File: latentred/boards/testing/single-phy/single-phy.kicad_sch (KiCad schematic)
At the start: 79 parts, among them J1 XILINX_JTAG, J2 RJ45, J3 QSH-030-01-L-D-A, U1 DP83867, U2 25MHZ_TBD, U3 BEL_FUSE_S558-5999-M8-F, U4 LTC3374-QFN

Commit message: single-phy: updated for v0.2 with fixed RJ45 pinout, removed SGMII clock pair, moved digital IO to 1.8V
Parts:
- removed C1, C2: 27p, azonenberg_pcb:EIA_0402_CAP_NOSILK, symbol device:C
- removed C13, C14: 0.1 uF, azonenberg_pcb:EIA_0402_CAP_NOSILK, symbol device:C
- removed L1: FERRITE_600R, azonenberg_pcb:EIA_0603_INDUCTOR_NOSILK, symbol passive-azonenberg:INDUCTOR_PWROUT
- added Q1, Q2: SSM6N58NU, azonenberg_pcb:DFN_6_0.65MM_2x2MM_GDS, symbol special-azonenberg:SSM6N58NU_DUAL_NMOS
- added R23: 33, azonenberg_pcb:EIA_0402_RES_NOSILK, symbol device:R
- added R24: 100, azonenberg_pcb:EIA_0402_RES_NOSILK, symbol device:R
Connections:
- net A2V5 is gone; now on net 2V5: C15.1, C19.1, C26.1, U1.3 (A2V5), U1.9 (A2V5)
- net PHY_CLK_25MHZ_DIV is gone; now on net PHY_CLK_25MHZ: U1.15 (XI)
- net SGMII_CLKOUT_N is gone; now on net SGMII_TX_N: J3.26 (DQ14_P)
- net SGMII_CLKOUT_P is gone; now on net SGMII_TX_P: J3.28 (DQ14_N)
- net 1V8: now also C18.1, C22.1, C25.1, C28.1, C30.1, J1.2 (Vccaux), R1.1, R12.2, R14.2, R22.2, R6.2, U1.19 (VCCIO), U1.30 (VCCIO), U1.41 (VCCIO), U2.1 (E/D#), U2.4 (Vdd)
- net 2V5: no longer C18.1, C22.1, C25.1, C28.1, C30.1, J1.2 (Vccaux), R1.1, R12.2, R14.2, R22.2, R6.2, U1.19 (VCCIO), U1.30 (VCCIO), U1.41 (VCCIO), U2.1 (E/D#), U2.4 (Vdd)
- net ETH_MDI_A_N: now also J2.2; no longer J2.5
- net ETH_MDI_A_P: now also J2.1; no longer J2.4
- net ETH_MDI_B_N: now also J2.6; no longer J2.2
- net ETH_MDI_B_P: now also J2.3; no longer J2.1
- net ETH_MDI_C_N: now also J2.5; no longer J2.6
- net ETH_MDI_C_P: now also J2.4; no longer J2.3
- net GND: now also Q1.S1 (S), Q1.S2 (S), Q2.D2 (D), Q2.G2 (G), Q2.S1 (S), Q2.S2 (S)
- net LED_0: now also Q1.G1 (G); no longer D3.2 (A)
- net LED_1: now also Q1.G2 (G); no longer D2.2 (A)
- net LED_2: now also Q2.G1 (G); no longer D1.2 (A)
- net MGMT_MDC: now also J3.22 (DQ13_N); no longer J3.58 (DQ19_N)
- net MGMT_MDIO: now also J3.20 (DQ13_P); no longer J3.56 (DQ19_P)
- net PHY_CLK_25MHZ: now also R23.2; no longer U2.3 (CLK)
- net SGMII_CLKOUT_AC_N: now also R24.1
- net SGMII_CLKOUT_AC_P: now also R24.2
- net SGMII_TX_N: no longer J3.38 (DQ16_P)
- net SGMII_TX_P: no longer J3.40 (DQ16_N)
- new net: D2.2 (A), Q1.D2 (D)
- new net: D3.2 (A), Q2.D1 (D)
- new net: D1.2 (A), Q1.D1 (D)
- new net: R23.1, U2.3 (CLK)
- no-connect marks 45 -> 47
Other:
- note added: "All SGMII pairs inverted for routability"
- note removed: "All SGMII pairs including clock inverted for routability"
- moved on the sheet: D1, D2, D3, R3, R4, R5

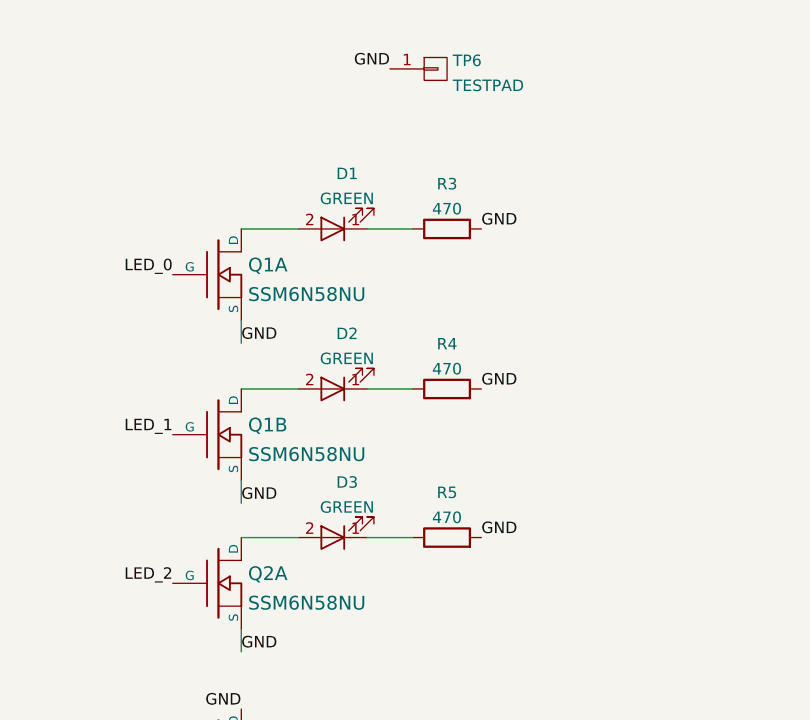
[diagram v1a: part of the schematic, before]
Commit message: Fixed incorrect LED level shifter connections
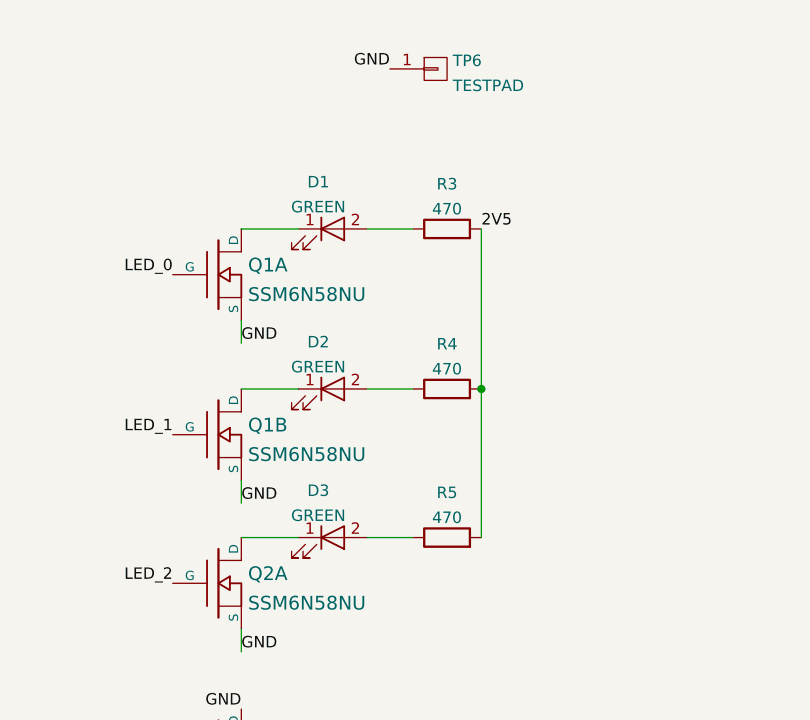
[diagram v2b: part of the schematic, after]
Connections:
- net 2V5: now also R3.2, R4.2, R5.2
- net GND: no longer R3.2, R4.2, R5.2
- net at R5.1: now also D3.2 (A); no longer D3.1 (K)
- net at D2.1 (K): now also Q1.D2 (D); no longer R4.1
- net at D2.2 (A): now also R4.1; no longer Q1.D2 (D)
- net at R3.1: now also D1.2 (A); no longer D1.1 (K)
- net at Q2.D1 (D): now also D3.1 (K); no longer D3.2 (A)
- net at Q1.D1 (D): now also D1.1 (K); no longer D1.2 (A)
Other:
- moved on the sheet: D1, D2, D3
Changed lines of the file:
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@@
   (junction (at 58.42 199.39) (diameter 0) (color 0 0 0 0)
+  )
+  (junction (at 290.83 218.44) (diameter 0) (color 0 0 0 0)
   )
   (junction (at 393.7 40.64) (diameter 0) (color 0 0 0 0)
@@
     (stroke (width 0) (type default) (color 0 0 0 0))
   )
+  (wire (pts (xy 290.83 200.66) (xy 290.83 218.44))
+    (stroke (width 0) (type default) (color 0 0 0 0))
+  )
   (wire (pts (xy 201.93 214.63) (xy 214.63 214.63))
     (stroke (width 0) (type default) (color 0 0 0 0))
@@
   )
   (wire (pts (xy 278.13 218.44) (xy 283.21 218.44))
+    (stroke (width 0) (type default) (color 0 0 0 0))
+  )
+  (wire (pts (xy 290.83 218.44) (xy 290.83 234.95))
     (stroke (width 0) (type default) (color 0 0 0 0))
   )
@@
     (effects (font (size 1.27 1.27)) (justify right bottom))
   )
-  (label "GND" (at 290.83 218.44 0)
-    (effects (font (size 1.27 1.27)) (justify left bottom))
-  )
   (label "ETH_MDI_B_P" (at 217.17 49.53 0)
     (effects (font (size 1.27 1.27)) (justify left bottom))
@@
     (effects (font (size 1.27 1.27)) (justify right bottom))
   )
-  (label "GND" (at 290.83 200.66 0)
+  (label "2V5" (at 290.83 200.66 0)
     (effects (font (size 1.27 1.27)) (justify left bottom))
   )
@@
   (label "GND" (at 264.16 254 180)
     (effects (font (size 1.27 1.27)) (justify right bottom))
-  )
-  (label "GND" (at 290.83 234.95 0)
-    (effects (font (size 1.27 1.27)) (justify left bottom))
   )
   (label "1V8" (at 49.53 35.56 180)
@@
     (pin "2")
   )
-  (symbol (lib_id "device:LED") (at 274.32 218.44 180) (unit 1)
-    (in_bom yes) (on_board yes) (fields_autoplaced)
-    (property "Reference" "D2" (id 0) (at 275.9202 212.3145 0))
-    (property "Value" "GREEN" (id 1) (at 275.9202 215.0896 0))
+  (symbol (lib_id "device:LED") (at 274.32 218.44 0) (unit 1)
+    (in_bom yes) (on_board yes) (fields_autoplaced)
+    (property "Reference" "D2" (id 0) (at 272.7198 213.2289 0))
+    (property "Value" "GREEN" (id 1) (at 272.7198 216.004 0))
     (property "Footprint" "azonenberg_pcb:EIA_0603_LED" (id 2) (at 274.32 218.44 0)
       (effects (font (size 1.27 1.27)) hide)
@@
     (pin "2")
   )
-  (symbol (lib_id "device:LED") (at 274.32 234.95 180) (unit 1)
-    (in_bom yes) (on_board yes) (fields_autoplaced)
-    (property "Reference" "D3" (id 0) (at 275.9202 228.8245 0))
-    (property "Value" "GREEN" (id 1) (at 275.9202 231.5996 0))
+  (symbol (lib_id "device:LED") (at 274.32 234.95 0) (unit 1)
+    (in_bom yes) (on_board yes) (fields_autoplaced)
+    (property "Reference" "D3" (id 0) (at 272.7198 229.7389 0))
+    (property "Value" "GREEN" (id 1) (at 272.7198 232.514 0))
     (property "Footprint" "azonenberg_pcb:EIA_0603_LED" (id 2) (at 274.32 234.95 0)
       (effects (font (size 1.27 1.27)) hide)
@@
     (pin "2")
   )
-  (symbol (lib_id "device:LED") (at 274.32 200.66 180) (unit 1)
-    (in_bom yes) (on_board yes) (fields_autoplaced)
-    (property "Reference" "D1" (id 0) (at 275.9202 194.5345 0))
-    (property "Value" "GREEN" (id 1) (at 275.9202 197.3096 0))
+  (symbol (lib_id "device:LED") (at 274.32 200.66 0) (unit 1)
+    (in_bom yes) (on_board yes) (fields_autoplaced)
+    (property "Reference" "D1" (id 0) (at 272.7198 195.4489 0))
+    (property "Value" "GREEN" (id 1) (at 272.7198 198.224 0))
     (property "Footprint" "azonenberg_pcb:EIA_0603_LED" (id 2) (at 274.32 200.66 0)
       (effects (font (size 1.27 1.27)) hide)

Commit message: Adding old LATENTRED design stuff that never got pushed
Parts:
- added C1, C13, C14, C2, C38, C39: C1005X7R1C104K050BC, symbol device:C
- added C40: 10 uF, azonenberg_pcb:EIA_0805_CAP_NOSILK, symbol device:C
- added C41, C42, C44, C45: 47 uF, azonenberg_pcb:EIA_1210_CAP_NOSILK, symbol device:C
- added C43, C46: 47 uF, symbol device:C
- added C47, C48: 4.7 uF, azonenberg_pcb:EIA_0603_CAP_NOSILK, symbol device:C
- added FB1, FB2: BLM31KN271SH1L, azonenberg_pcb:EIA_1206_CAP_NOSILK, symbol passive-azonenberg:FERRITE_SMALL2
- added L1: FERRITE, symbol passive-azonenberg:INDUCTOR_PWROUT
- added TP7, TP8, TP9: U.FL, azonenberg_pcb:CONN_U.FL_TE_1909763-1, symbol conn:CONN_COAXIAL
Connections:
- net 1V0: now also C2.1
- net 1V8: now also C1.1, C41.1, C42.1, FB1.1, FB2.1; no longer C17.1, C18.1, C21.1, C22.1, C24.1, C25.1, C28.1, U1.13 (A1V8), U1.19 (VCCIO), U1.30 (VCCIO), U1.41 (VCCIO), U1.48 (A1V8)
- net 2V5: now also C13.1
- net 5V0: now also C14.2, C38.2, C39.2, C40.1, C43.1, C46.1, L1.1, TP7.1 (In); no longer J3.59 (5V0), J3.60 (5V0)
- net GND: now also C1.2, C13.2, C14.1, C2.2, C38.1, C39.1, C40.2, C41.2, C42.2, C43.2, C44.2, C45.2, C46.2, C47.2, C48.2, TP7.2 (Ext), TP8.2 (Ext), TP9.2 (Ext)
- new net 5V0_RAW: J3.59 (5V0), J3.60 (5V0), L1.2
- new net A1V8: C17.1, C21.1, C24.1, C44.1, C47.1, FB1.2, TP8.1 (In), U1.13 (A1V8), U1.48 (A1V8)
- new net D1V8: C18.1, C22.1, C25.1, C28.1, C45.1, C48.1, FB2.2, TP9.1 (In), U1.19 (VCCIO), U1.30 (VCCIO), U1.41 (VCCIO)
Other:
- moved on the sheet: TP2, TP3, TP4, TP6
